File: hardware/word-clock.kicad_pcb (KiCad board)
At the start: 2 copper layers, 177.8 x 177.8 mm, 55 parts, among them SW1 Hour, SW2 Minute, SW3 Audio, U1 ESP32 CP2102, U2 74HC245

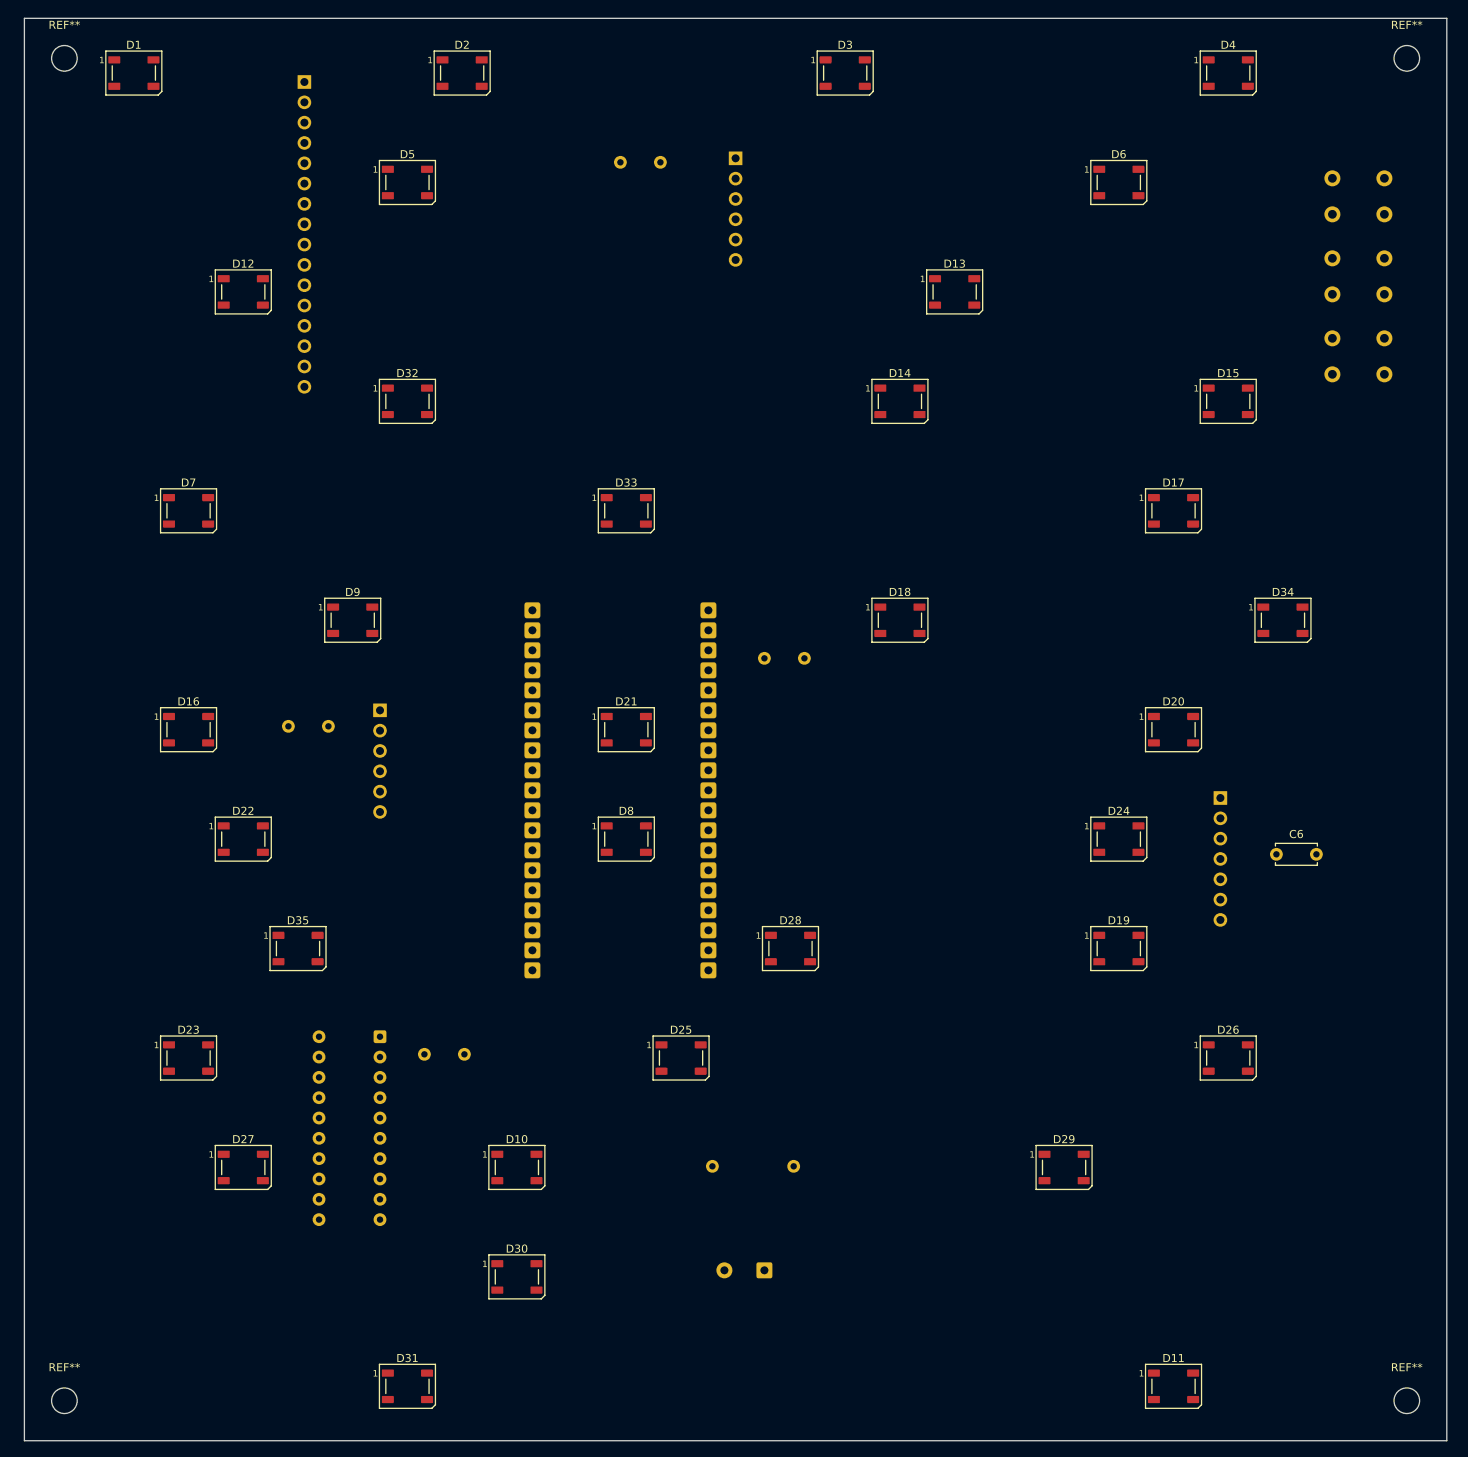
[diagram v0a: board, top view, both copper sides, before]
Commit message: feat(hardware): led chain reorder, AT relocated, routing + pour complete
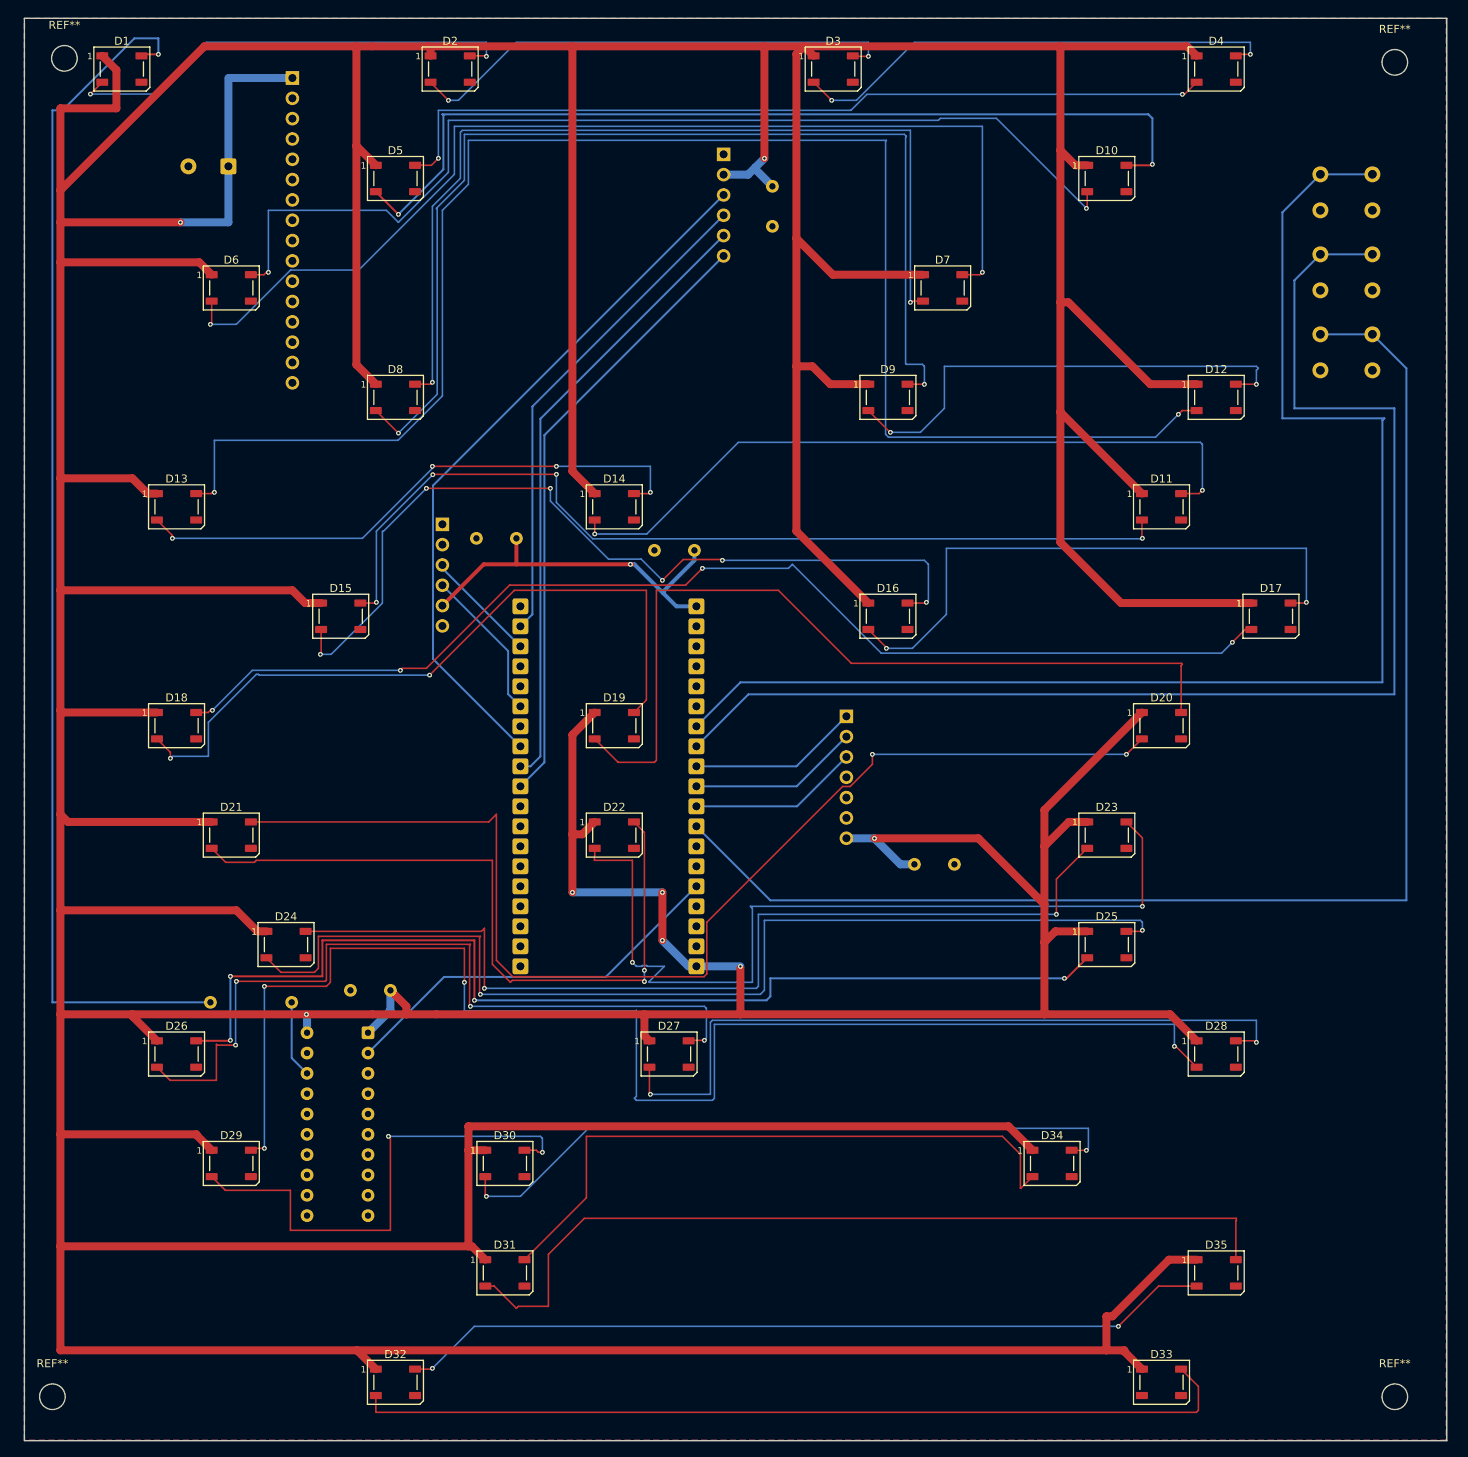
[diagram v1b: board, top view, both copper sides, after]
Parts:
- C3: renamed from C6; moved to B.Cu
- moved C2 153.4 mm to (25.5, 18.5)
- moved D35 66.9 mm to (149.0, 156.8)
- moved R1 66.0 mm to (33.4, 123.0)
- moved J_AMP1 47.9 mm to (102.8, 87.2)
- moved C3 40.3 mm to (116.2, 105.8), turned to 180 degrees
- moved C4 33.2 mm to (61.5, 65.0)
- moved J_RTC1 24.5 mm to (52.2, 63.2)
- moved C1 19.3 mm to (83.8, 66.5)
- moved C5 16.1 mm to (93.5, 26.0), turned to 90 degrees
- moved C6 12.2 mm to (45.8, 121.5)
- moved D1 1.58 mm to (12.2, 6.34)
- moved D10 1.58 mm to (135.3, 20.0)
- moved D11 1.58 mm to (142.1, 61.1)
- moved D12 1.58 mm to (149.0, 47.4)
- moved D13 1.58 mm to (19.0, 61.1)
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- renumbered C2 to C1, C7 to C2, C5 to C4, C4 to C5, C3 to C6, D6 to D10, D17 to D11, D15 to D12, D7 to D13, D33 to D14, D9 to D15, D18 to D16, D34 to D17, D16 to D18, D21 to D19, D22 to D21, D8 to D22, D24 to D23, D35 to D24, D19 to D25, D23 to D26, D25 to D27, D26 to D28, D27 to D29, D10 to D30, D30 to D31, D31 to D32, D11 to D33, D29 to D34, D28 to D35, D12 to D6, D13 to D7, D32 to D8, D14 to D9, SW2 to SW1, SW3 to SW2, SW1 to SW3
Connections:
- D11 pad 2: Net-(D17-DOUT) -> Net-(D11-DOUT)
- D11 pad 4: Net-(D16-DOUT) -> Net-(D11-DIN)
- D13 pad 2: Net-(D16-DIN) -> Net-(D13-DOUT)
- D14 pad 2: Net-(D33-DOUT) -> Net-(D11-DIN)
- D14 pad 4: Net-(D32-DOUT) (its old number) -> Net-(D13-DOUT)
- D15 pad 2: Net-(D24-DIN) -> Net-(D15-DOUT)
- D15 pad 4: Net-(D23-DOUT) -> Net-(D11-DOUT)
- D16 pad 2: Net-(D18-DOUT) -> Net-(D16-DOUT)
- D16 pad 4: Net-(D17-DOUT) -> Net-(D15-DOUT)
- D17 pad 2: Net-(D34-DOUT) -> Net-(D17-DOUT)
- D17 pad 4: Net-(D33-DOUT) -> Net-(D16-DOUT)
- D18 pad 2: Net-(D16-DOUT) -> Net-(D18-DOUT)
- D18 pad 4: Net-(D16-DIN) -> Net-(D17-DOUT)
- D19 pad 2: Net-(D21-DOUT) -> Net-(D19-DOUT)
- D19 pad 4: Net-(D20-DOUT) -> Net-(D18-DOUT)
- D20 pad 4: Net-(D20-DIN) -> Net-(D19-DOUT)
- D21 pad 2: Net-(D22-DOUT) -> Net-(D21-DOUT)
- D21 pad 4: Net-(D21-DOUT) -> Net-(D20-DOUT)
- D22 pad 2: Net-(D20-DIN) -> Net-(D22-DOUT)
- D22 pad 4: Net-(D19-DOUT) -> Net-(D21-DOUT)
- D23 pad 2: Net-(D24-DOUT) -> Net-(D23-DOUT)
- D23 pad 4: Net-(D24-DIN) -> Net-(D22-DOUT)
- D24 pad 2: unconnected-(D35-DOUT-Pad2) -> Net-(D24-DOUT)
- D24 pad 4: Net-(D34-DOUT) -> Net-(D23-DOUT)
- D25 pad 2: Net-(D19-DOUT) -> Net-(D25-DOUT)
- D25 pad 4: Net-(D18-DOUT) -> Net-(D24-DOUT)
- D26 pad 2: Net-(D23-DOUT) -> Net-(D26-DOUT)
- D26 pad 4: Net-(D22-DOUT) -> Net-(D25-DOUT)
- D27 pad 4: Net-(D24-DOUT) -> Net-(D26-DOUT)
- D30 pad 2: Net-(D10-DOUT) (its old number) -> Net-(D30-DOUT)
- D31 pad 2: Net-(D30-DOUT) -> Net-(D31-DOUT)
- D32 pad 4: Net-(D30-DOUT) -> Net-(D32-DIN)
- D33 pad 2: Net-(D11-DOUT) -> unconnected-(D33-DOUT-Pad2)
- D34 pad 4: Net-(D28-DOUT) (its old number) -> Net-(D30-DOUT)
- D35 pad 2: Net-(D28-DOUT) (its old number) -> Net-(D32-DIN)
- D35 pad 4: Net-(D10-DOUT) (its old number) -> Net-(D31-DOUT)
- D7 pad 2: Net-(D13-DOUT) -> Net-(D7-DOUT)
- D8 pad 2: Net-(D32-DOUT) (its old number) -> Net-(D8-DOUT)
- D8 pad 4: Net-(D11-DOUT) -> Net-(D7-DOUT)
- D9 pad 4: Net-(D13-DOUT) -> Net-(D8-DOUT)
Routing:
- net +5V: track 0.00 -> 1486.3 mm, vias 0 -> 8
- net Net-(D12-DOUT): track 0.00 -> 202.4 mm, vias 0 -> 2
- net Net-(D28-DOUT): track 0.00 -> 175.5 mm, vias 0 -> 4
- net /BTN_HOUR: track 0.00 -> 172.8 mm
- net /BTN_AUDIO: track 0.00 -> 171.6 mm
- net /BTN_MINUTE: track 0.00 -> 165.3 mm
- net /LED_DATA_OUT: track 0.00 -> 152.4 mm, vias 0 -> 1
- net Net-(D20-DOUT): track 0.00 -> 147.7 mm, vias 0 -> 2
- net Net-(D17-DOUT): track 0.00 -> 145.4 mm, vias 0 -> 4
- net Net-(D8-DOUT): track 0.00 -> 135.5 mm, vias 0 -> 2
- net Net-(D25-DOUT): track 0.00 -> 135.5 mm, vias 0 -> 4
- net Net-(D6-DOUT): track 0.00 -> 134.1 mm, vias 0 -> 2
- net Net-(D24-DOUT): track 0.00 -> 133.9 mm, vias 0 -> 2
- net Net-(D10-DOUT): track 0.00 -> 129.3 mm, vias 0 -> 2
- net Net-(D23-DOUT): track 0.00 -> 120.5 mm, vias 0 -> 2
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- added copper zone on B.Cu, net GND
- added copper zone on F.Cu, net GND

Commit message: fix(hardware): remove cermant usb-c breakout, power via esp32 micro-usb
Removes J_USB1 from the schematic and PCB. The user-facing USB-C port on
the back panel will now be provided by a panel-mount USB-C-female-to-
micro-USB-male pigtail plugged directly into the ESP32 module's native
micro-USB connector. The CP2102 bridge on the module handles both power
and firmware flashing — one port, one hole in the back panel, no PCB
data-routing rework needed.

PWR_FLAG on +5V re-attached to the module's 5V pin to satisfy ERC.

Downstream docs updated:
- pinout.md Power/Input line now describes the new path.
- phase-2-parts-list.md marks the old USB-C breakout as superseded on the
  final PCB (still useful for breadboard bring-up) and adds the panel-
  mount pigtail as its own line item.

Open: when the AITRIP ESP32 modules arrive, inspect the micro-USB input
for a polyfuse. If a 500 mA fuse is present it will nuisance-trip under
LEDs + audio — bridge or replace before fab.
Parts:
- removed J_USB1: USB-C breakout (Cermant 16P), Connector_PinHeader_2.54mm:PinHeader_1x16_P2.54mm_Vertical
- removed the REF** at (171.3, 5.50)
- removed the REF** at (3.50, 172.3)
- removed the REF** at (171.3, 172.3)
- added REF**: MountingHole_3.2mm_M3, MountingHole:MountingHole_3.2mm_M3, F.Cu at (172.3, 172.3)
- added REF**: MountingHole_3.2mm_M3, MountingHole:MountingHole_3.2mm_M3, F.Cu at (5.00, 172.3)
- added REF**: MountingHole_3.2mm_M3, MountingHole:MountingHole_3.2mm_M3, F.Cu at (172.3, 5.50)
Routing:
- net +5V: track 1486.3 -> 1467.2 mm

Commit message: fix(hardware): swap J_RTC1 and J_SD1 to right-angle female sockets
DS3231 (HW-084) and HW-125 modules ship with right-angle pins that
don't fit into vertical through-hole sockets without bending. Swap the
PCB footprints from PinHeader_1x06_P2.54mm_Vertical to
PinSocket_1x06_P2.54mm_Horizontal so the daughterboards plug directly
in with the modules lying parallel to the main PCB.

Pad global positions preserved in both footprints so existing routing
is unchanged. J_SD1 keeps rot=180 with Y-mirrored coords (body extends
east into clear space); J_RTC1 uses rot=0 with un-mirrored coords
(body extends west, away from ESP32 at +X).

Also gitignore *.xlsx and word-clock-gerbers-*.zip so generated PCBA
artifacts don't pollute the repo (consistent with existing .gbr/.csv
rules).
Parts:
- J_RTC1, J_SD1: footprint Connector_PinHeader_2.54mm:PinHeader_1x06_P2.54mm_Vertical -> Connector_PinSocket_2.54mm:PinSocket_1x06_P2.54mm_Horizontal
- moved C5 16.3 mm to (77.5, 23.0)
- turned J_RTC1 to 0 degrees
- renumbered REF** to H1, REF** to H2, REF** to H3, REF** to H4
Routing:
- net +5V: track 1467.2 -> 1463.8 mm, vias 8 -> 7
